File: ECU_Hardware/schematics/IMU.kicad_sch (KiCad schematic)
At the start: 0 parts

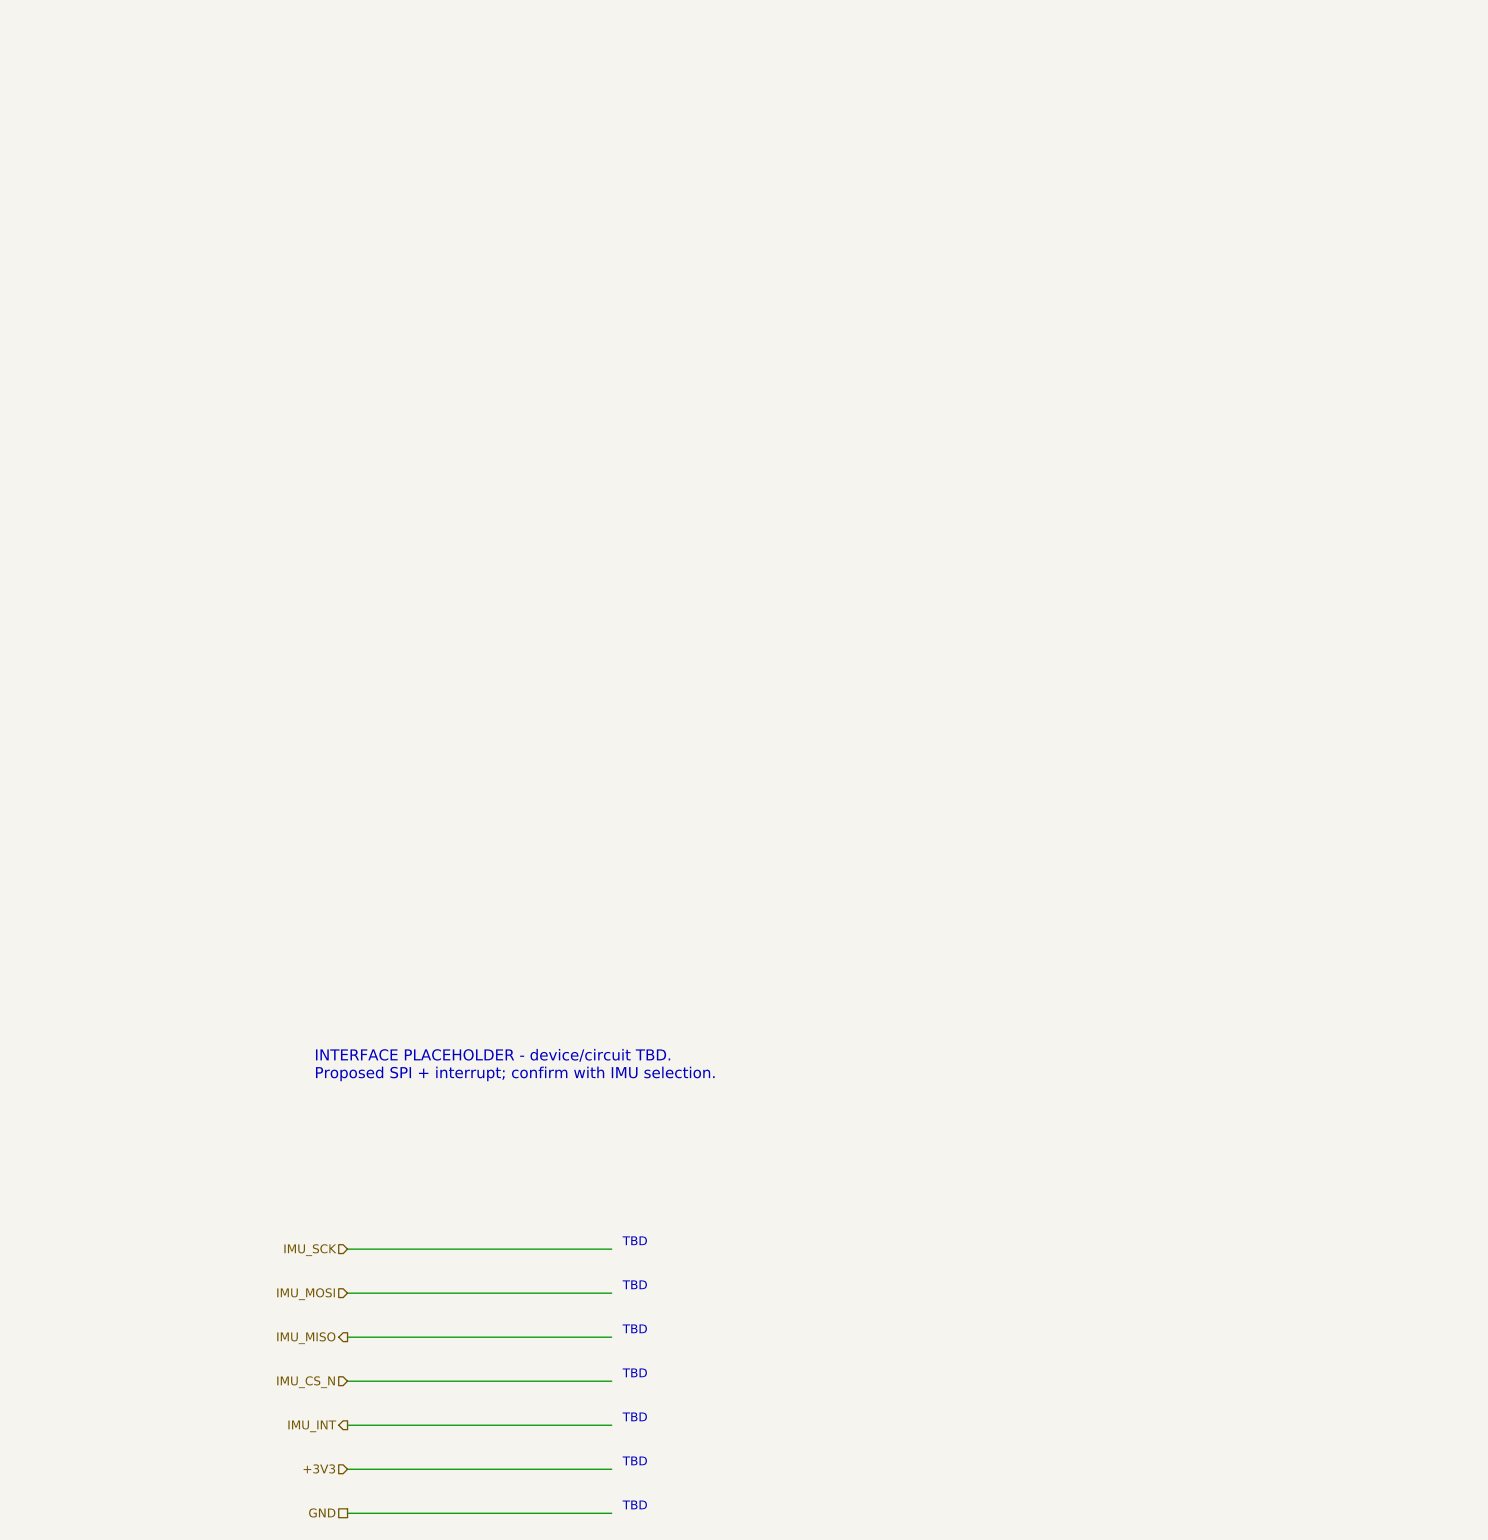
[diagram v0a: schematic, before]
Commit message: Move ECU schematics into schematics/ and add driver inputs and sensor notes
Hierarchical sheets now live in ECU_Hardware/schematics, with the new
Driver_Inputs sheet (APPS, BPPS and steering dividers and clamps), the
reviewed and JLCPCB project symbol libraries, new 3D models, and
SENSOR_INTERFACES.md with the GPS, IMU and temperature pin allocation.
The old top-level sheets and the restore backup are removed.

Claude-Session: https://claude.ai/code/session_0117trEbCv7z6CPYkN3K3GKQ
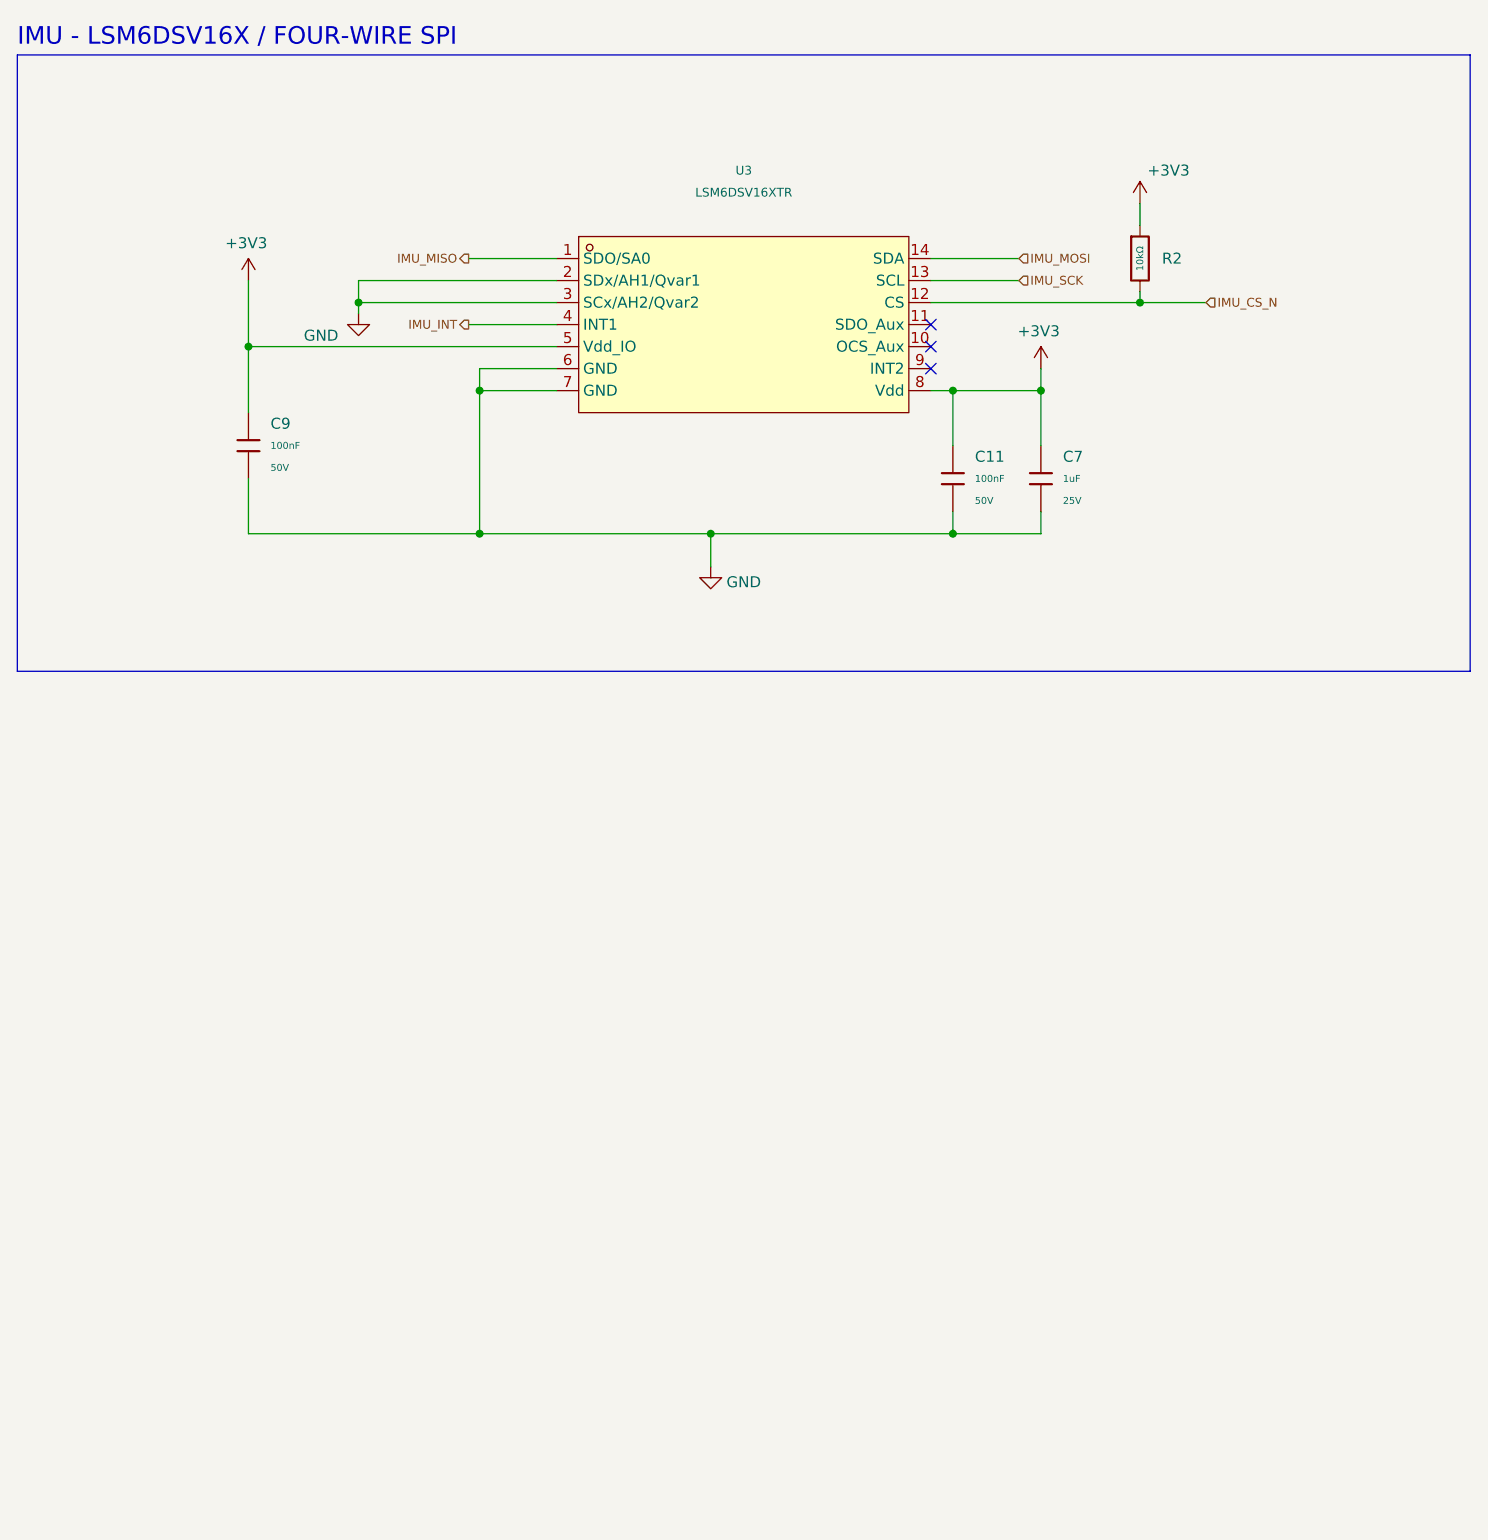
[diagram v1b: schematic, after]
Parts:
- added C11, C9: 100nF, PCM_JLCPCB:C_0402, symbol PCM_JLCPCB-Capacitors:0402,100nF,(2)
- added C7: 1uF, PCM_JLCPCB:C_0402, symbol PCM_JLCPCB-Capacitors:0402,1uF
- added R2: 10kΩ, PCM_JLCPCB:R_0402, symbol PCM_JLCPCB-Resistors:0402,10kΩ
- added U3: LSM6DSV16XTR, easyeda2kicad:LGA-14_L3.0-W2.5-P0.50-BR, symbol ECU_Reviewed:LSM6DSV16XTR
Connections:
- net +3V3: now also C11.1, C7.1, C9.1, R2.1, U3.5 (Vdd_IO), U3.8 (Vdd)
- net GND: now also C11.2, C7.2, C9.2, U3.2 (SDx/AH1/Qvar1), U3.3 (SCx/AH2/Qvar2), U3.6 (GND), U3.7 (GND)
- net IMU_CS_N: now also R2.2, U3.12 (CS)
- net IMU_INT: now also U3.4 (INT1)
- net IMU_MISO: now also U3.1 (SDO/SA0)
- net IMU_MOSI: now also U3.14 (SDA)
- net IMU_SCK: now also U3.13 (SCL)
- no-connect marks 0 -> 3
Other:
- note added: "IMU - LSM6DSV16X / FOUR-WIRE SPI"
- note removed: "INTERFACE PLACEHOLDER - device/circuit TBD. Proposed SPI + interrupt; confirm with IMU selection."
- note removed: "TBD"
